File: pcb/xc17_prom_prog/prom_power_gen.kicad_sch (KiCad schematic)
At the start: 100 parts, among them U10 LM317, U11 LM317, U12 LM317, U13 MC33063AD, U14 MC33063AD, U6 LM317, U7 LM317, U8 LM317, U9 LM317

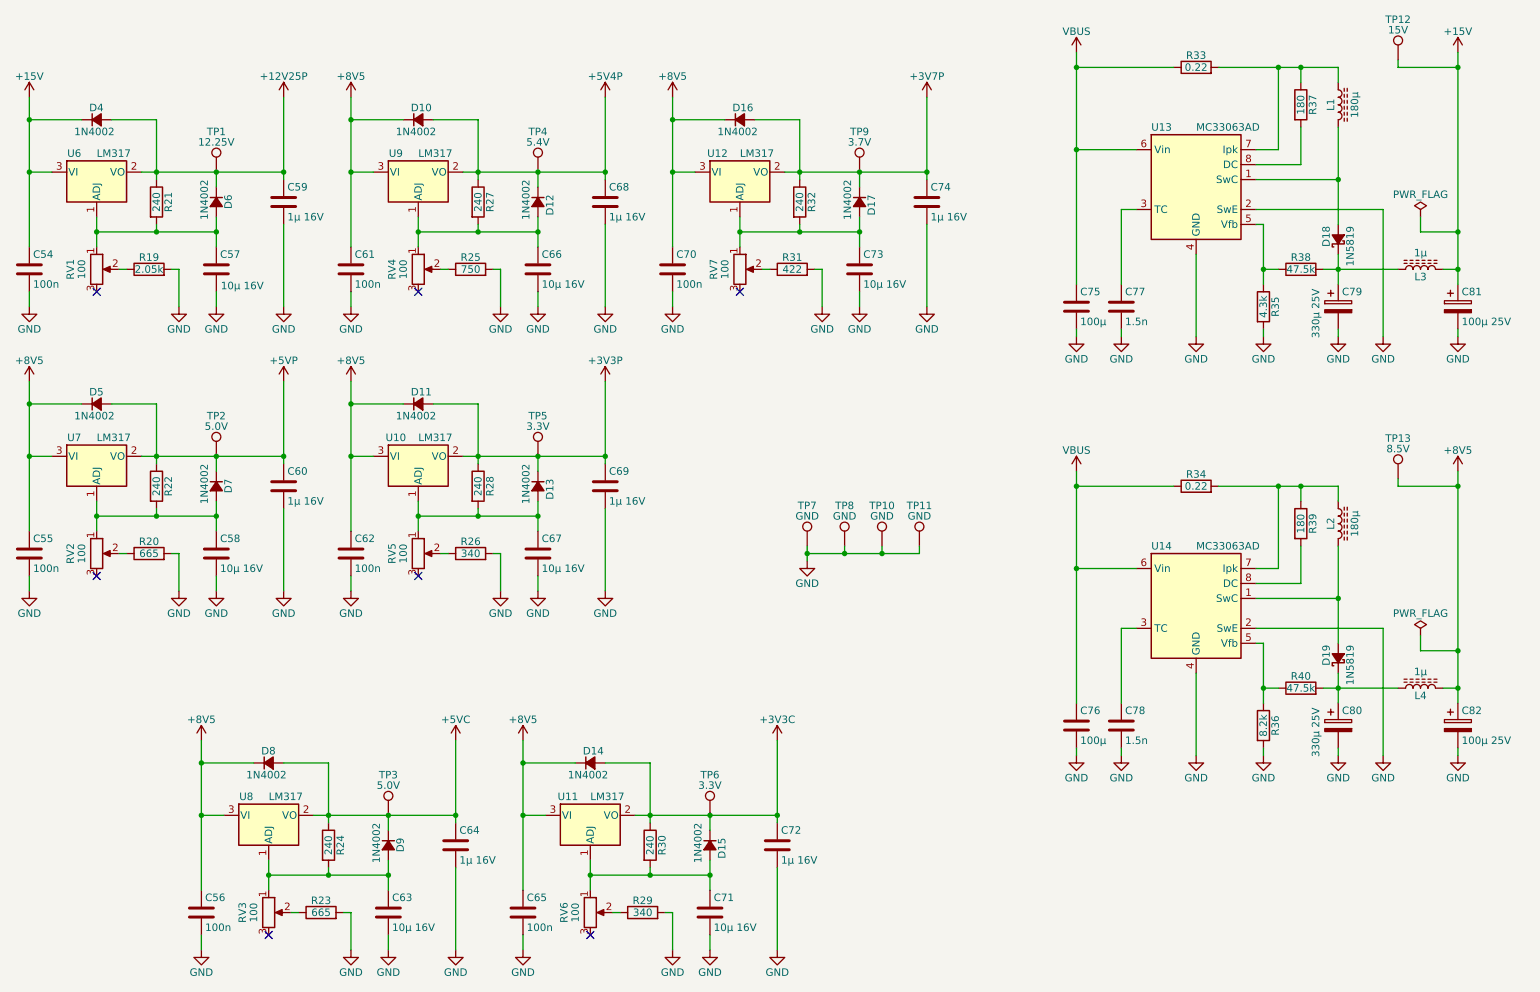
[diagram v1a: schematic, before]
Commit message: Migrate from HX1K to HX4K FPGA
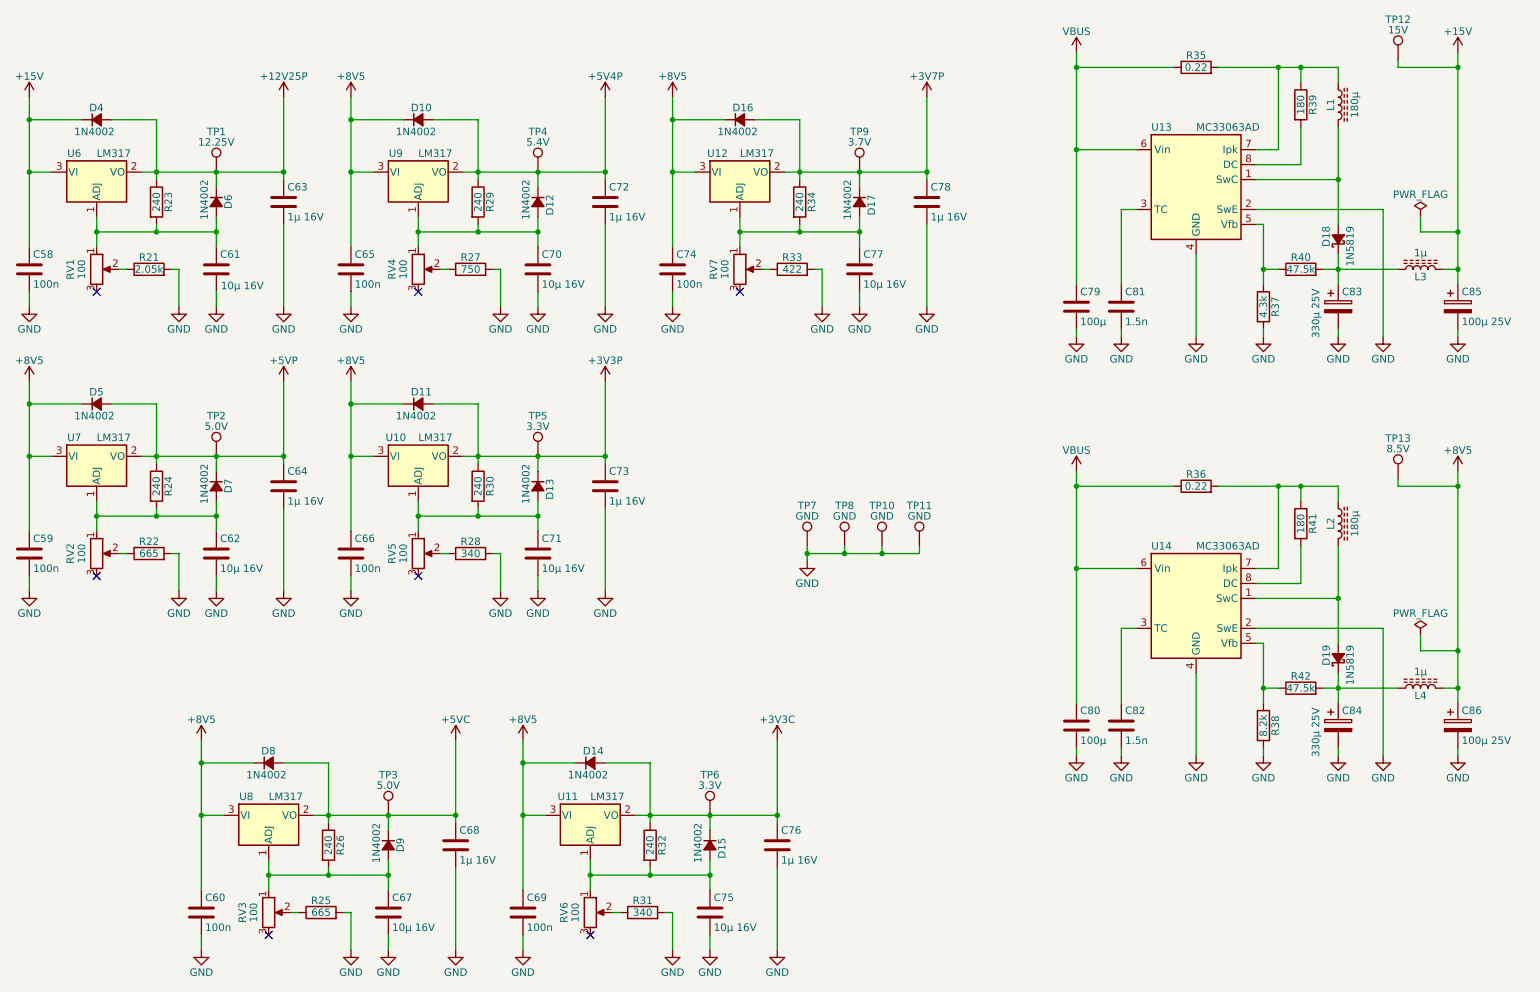
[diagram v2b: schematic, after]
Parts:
- renumbered C54 to C58, C55 to C59, C56 to C60, C57 to C61, C58 to C62, C59 to C63, C60 to C64, C61 to C65, C62 to C66, C63 to C67, C64 to C68, C65 to C69, C66 to C70, C67 to C71, C68 to C72, C69 to C73, C70 to C74, C71 to C75, C72 to C76, C73 to C77, C74 to C78, C75 to C79, C76 to C80, C77 to C81, C78 to C82, C79 to C83, C80 to C84, C81 to C85, C82 to C86, R19 to R21, R20 to R22, R21 to R23, R22 to R24, R23 to R25, R24 to R26, R25 to R27, R26 to R28, R27 to R29, R28 to R30, R29 to R31, R30 to R32, R31 to R33, R32 to R34, R33 to R35, R34 to R36, R35 to R37, R36 to R38, R37 to R39, R38 to R40, R39 to R41, R40 to R42
